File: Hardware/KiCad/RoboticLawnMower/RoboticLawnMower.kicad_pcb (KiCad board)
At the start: 4 copper layers, 100.1 x 100 mm, 192 parts, among them J1 MOTOR, J10 I2C 0, J11 Conn_01x02, J12 Conn_02x05_Row_Letter_Last, J13 I2C 0, J14 ADC 1, J15 ADC 2, J16 Conn_01x03, J17 Conn_01x03, J18 Conn_01x03, J19 RAIN, J2 MOTOR, J20 Dist 00, J21 Dist 01, J22 Dist 02, J3 MOTOR, J4 MOTOR, J5 MOTOR, J6 Coll 00, J7 Coll 01, J8 Coll 02, J9 GPS, Q1 BSS123, Q2 BSS123, Q3 Si7141DP, Q4 Si7141DP, Q5 Si7141DP, Q6 BSS123, Q7 Si7141DP, Q8 BSS123, U1 INA233, U10 INA233, U11 INA233, U12 INA233, U13 INA233, U14 STM32H573RITx, U2 LT1785AxS8, U20 TXB0102DCU, U21 TXB0102DCU, U22 TXB0102DCU, U23 TXB0102DCU, U24 TXB0102DCU, U25 TSR_1-2450, U3 mini_esp32, U4 PCA9685PW, U5 W25Q128JVS, U6 SRV05-4, U7 TSR_1-2450, U8 ADS1115IDGS, U9 ADS1115IDGS, Y2 32.768kHz

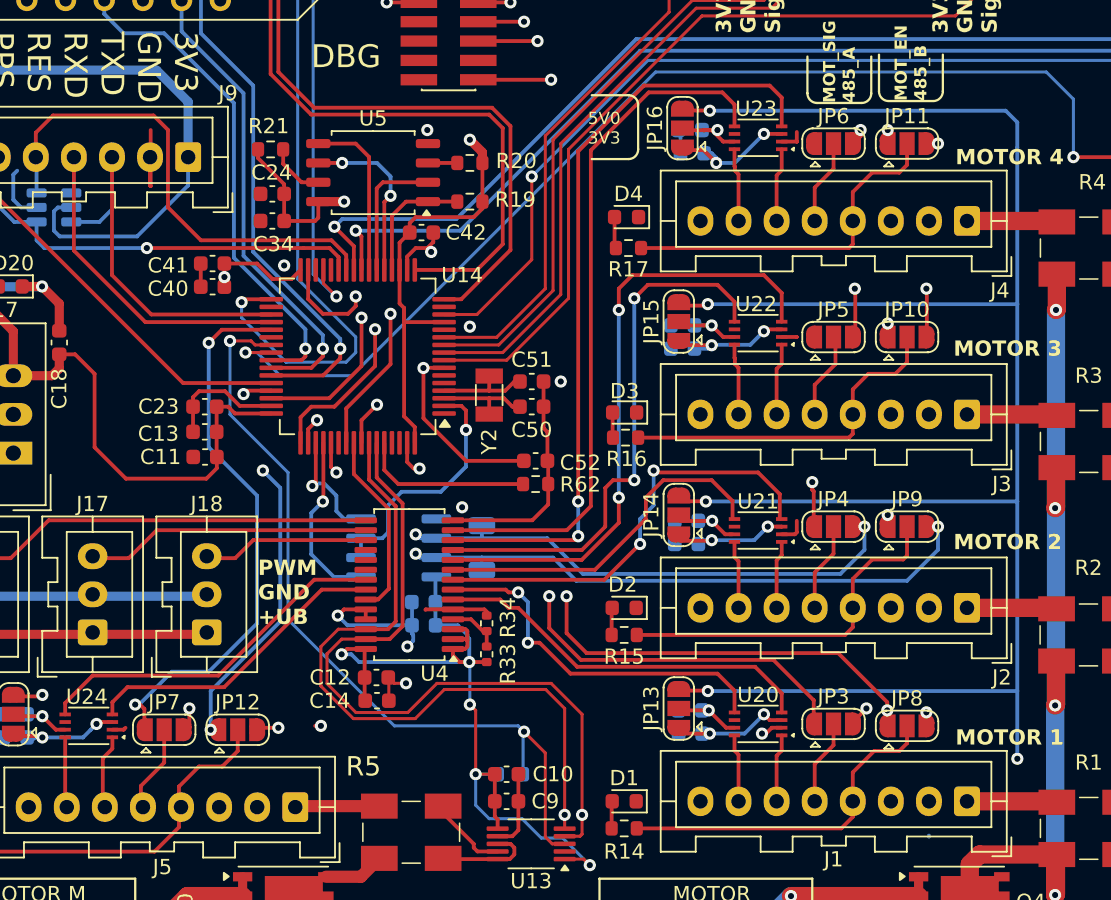
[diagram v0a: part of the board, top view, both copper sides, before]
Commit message: Levelshift für MotorSignal zum µC
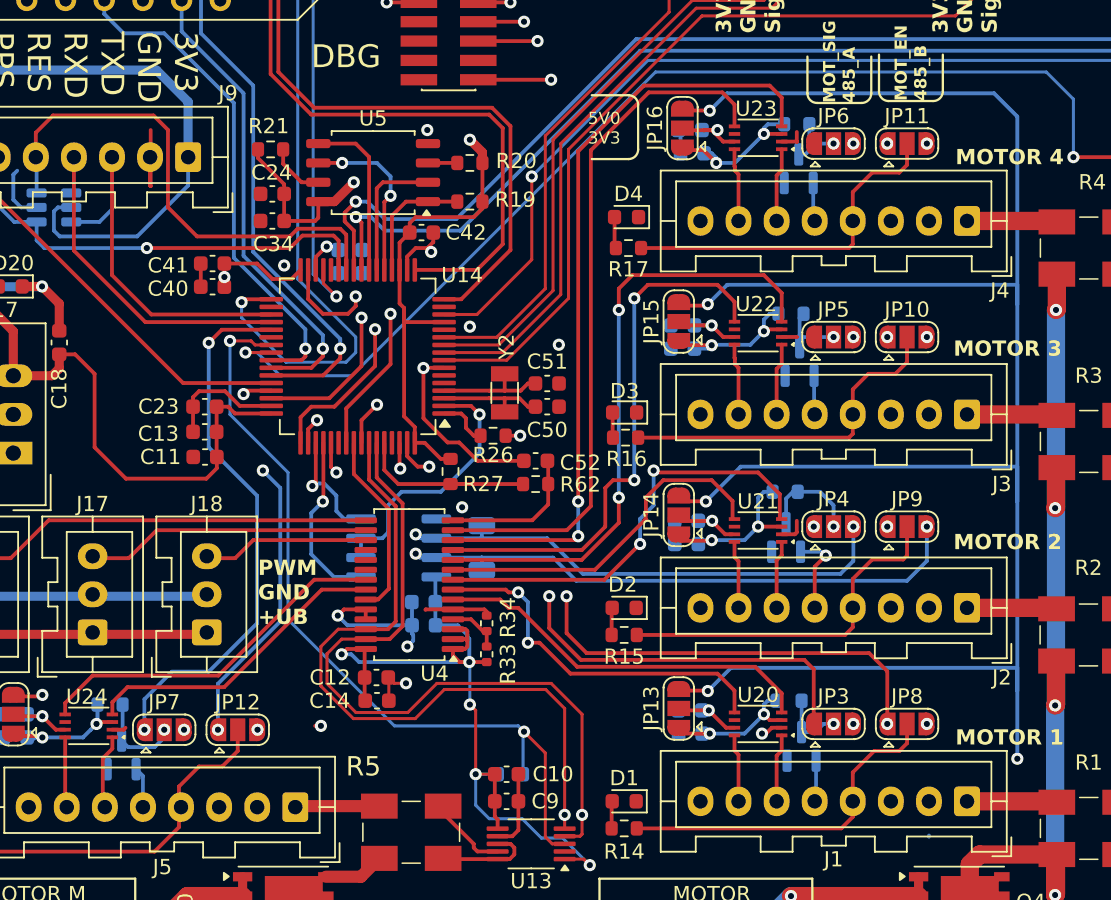
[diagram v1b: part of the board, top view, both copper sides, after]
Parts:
- added C25: 100n, Capacitor_SMD:C_0603_1608Metric, B.Cu at (127.1, 94.9)
- added C43: 2µ2, Capacitor_SMD:C_0603_1608Metric, B.Cu at (127.1, 93.3)
- added Q10: BSS123, Package_TO_SOT_SMD:SOT-23, B.Cu at (155.8, 112.2)
- added Q11: BSS123, Package_TO_SOT_SMD:SOT-23, B.Cu at (156.7, 100.7)
- added Q12: BSS123, Package_TO_SOT_SMD:SOT-23, B.Cu at (156.6, 88.0)
- added Q13: BSS123, Package_TO_SOT_SMD:SOT-23, B.Cu at (112.1, 126.5)
- added Q9: BSS123, Package_TO_SOT_SMD:SOT-23, B.Cu at (156.8, 125.9)
- added R26: N.C., Resistor_SMD:R_0603_1608Metric, F.Cu at (136.5, 105.5)
- added R27: N.C., Resistor_SMD:R_0603_1608Metric, F.Cu at (133.7, 107.9)
- added R28: 2k2, Resistor_SMD:R_0603_1608Metric, B.Cu at (156.0, 122.9)
- added R29: 2k2, Resistor_SMD:R_0603_1608Metric, B.Cu at (155.7, 109.2)
- added R30: 2k2, Resistor_SMD:R_0603_1608Metric, B.Cu at (156.1, 97.5)
- added R31: 2k2, Resistor_SMD:R_0603_1608Metric, B.Cu at (156.5, 85.1)
- added R32: 2k2, Resistor_SMD:R_0603_1608Metric, B.Cu at (111.4, 123.2)
- moved Y2 1.03 mm to (137.3, 102.7)
- moved C51 1.02 mm to (140.1, 102.1)
- moved C50 1.02 mm to (140.1, 103.6)
- moved JP8 0.13 mm to (163.7, 124.5)
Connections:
- JP3 pad 2: Net-(J1-Pin_5) -> Net-(JP3-C)
- JP4 pad 2: Net-(J2-Pin_5) -> Net-(JP4-C)
- JP5 pad 2: Net-(J3-Pin_5) -> Net-(JP5-C)
- JP6 pad 2: Net-(J4-Pin_5) -> Net-(JP6-C)
- JP7 pad 2: Net-(J5-Pin_5) -> Net-(JP7-C)
- U14 pad 1: unconnected-(U14-VBAT-Pad1) -> Net-(U14-VBAT)
- U14 pad 30: unconnected-(U14-VCAP-Pad30) -> Net-(C25-Pad1)
- U14 pad 62: unconnected-(U14-VCAP-Pad62) -> Net-(C25-Pad1)
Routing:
- net +3.3V: track 541.0 -> 517.2 mm, vias 29 -> 30
- net Net-(C25-Pad1): track 0.00 -> 23.3 mm, vias 0 -> 2
- net +5V: track 363.8 -> 372.2 mm
- net Net-(JP4-C): track 0.00 -> 6.68 mm, vias 0 -> 1
- net Net-(JP7-C): track 0.00 -> 6.13 mm, vias 0 -> 1
- net Net-(JP5-C): track 0.00 -> 5.36 mm, vias 0 -> 1
- net GND: track 405.9 -> 400.9 mm
- net Net-(JP3-C): track 0.00 -> 4.38 mm, vias 0 -> 1
- net Net-(JP6-C): track 0.00 -> 4.24 mm, vias 0 -> 1
- net /RS485_B: track 104.4 -> 100.4 mm
- net Net-(U14-VBAT): track 0.00 -> 3.37 mm
- net Net-(J3-Pin_5): track 5.64 -> 2.56 mm
- net Net-(J4-Pin_5): track 5.59 -> 2.53 mm
- net Net-(J5-Pin_5): track 5.59 -> 2.68 mm
- net Net-(J1-Pin_5): track 5.59 -> 2.70 mm
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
